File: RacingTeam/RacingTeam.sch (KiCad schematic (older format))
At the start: 78 parts, among them J1 BusIn, J10 BatteryIn, J11 ShutdownIn, J2 Conn_01x01, J3 Conn_01x01, J4 Conn_01x01, J5 Conn_01x01, J6 PreCharge Relay Out, J7 AIROut, J8 Discharge Relay Out, J9 PCB OUT, Q1 TP0610T, Q2 2N7002, Q3 2N7002, Q4 2N7002, Q5 2N7002, Q6 TP0610T, Q7 2N7002, Q8 TP0610T, U1 LM311, U2 LM311, U3 4N35, U6 NE555D

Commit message: Update RacingTeam.kicad_pcb, RacingTeam.kicad_pcb-bak, and 3 more files...
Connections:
- net PrechargeTP+ is gone; now on net PrechargeRef: D1.1 (K), F6.1, F6.2, J3.1 (Pin_1), R10.2, R11.1, R16.2
- net TSALREF: now also F2.2, R1.1, R2.2; no longer F2.1, J4.1 (Pin_1), R19.2
- net 555Reset: now reaches Q5.3 (D), Q6.1 (G), R27.2, U6.4 (R)
- net 555Trigger: now reaches C8.1, R30.2, U6.2 (TR), U6.6 (THR)
- net 555Ouput: now reaches Q7.2 (G), U6.3 (Q)
- net 555DischargePullup: now reaches R29.2, R30.1, U6.7 (DIS)
- net 555Drive: now reaches Q7.3 (D), Q8.1 (G), R31.2
- net OBLEDResistorRed: now reaches D8.1 (K), R32.1
- net OBLEDRed: now reaches D8.2 (A), JP2.2
- net TSALRef: now reaches F1.2, R14.2, R15.1
- net PrechargeRelayOut: now reaches D3.2 (A), J6.2 (Pin_2), R21.2
- net AIROut: now reaches D4.2 (A), J7.2 (Pin_2), R23.2
- net OBLEDResistorGreen: now reaches D6.1 (K), R28.1
- net OBLEDGreen: now reaches D6.2 (A), JP1.2
- net Ec3Out+: now reaches F3.2, PS1.6 (+VOUT)
- net DischargeIn: now reaches D5.1 (K), Q3.1 (S), Q4.1 (S)
- net DischargeIn: now also J8.2 (Pin_2); no longer J8.1 (Pin_1)
- net DischargeOut: now reaches D5.2 (A), R25.2
- net DischargeOut: now also J8.1 (Pin_1); no longer J8.2 (Pin_2)
- new net TSALCommon: F2.1, J4.1 (Pin_1), R19.2
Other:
- note added: "How drive?\n"
- moved on the sheet: F1, F3, R28, R32
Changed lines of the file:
@@
 	750  3300 750  3350
 Wire Wire Line
-	1300 2250 1400 2250
+	1300 2250 1450 2250
 Wire Wire Line
 	2300 2250 2300 2700
@@
 	1    0    0    -1
 $EndComp
-Text Label 1550 3300 0    25   ~ 0
+Text Label 750  3300 0    25   ~ 0
 TSALREF
 Text Label 1650 2250 0    25   ~ 0
@@
 Text Label 3400 3300 0    25   ~ 0
 LM311V-
-Text Label 3900 2600 1    25   ~ 0
-LM311Power+
-Text Label 4250 3350 2    25   ~ 0
-LM311Power-
 $Comp
 L RacingTeamPCB:C C3
@@
 	1    0    0    -1
 $EndComp
-Text Label 5150 2900 0    25   ~ 0
-OptoIn
 Text Label 4600 3000 0    25   ~ 0
 CompOut
@@
 L RacingTeamPCB:GLV- #U010
 U 1 1 623FD30F
-P 8500 4550
-F 0 "#U010" H 8422 4504 50  0001 R CNN
-F 1 "GLV-" H 8600 4400 50  0000 R CNN
-F 2 "" H 8500 4550 50  0001 C CNN
-F 3 "" H 8500 4550 50  0001 C CNN
-	1    8500 4550
+P 8500 4650
+F 0 "#U010" H 8422 4604 50  0001 R CNN
+F 1 "GLV-" H 8600 4500 50  0000 R CNN
+F 2 "" H 8500 4650 50  0001 C CNN
+F 3 "" H 8500 4650 50  0001 C CNN
+	1    8500 4650
 	1    0    0    -1
 $EndComp
@@
 	8650 5950 8650 6050
 Wire Wire Line
-	8650 6050 8900 6050
+	8650 6050 8800 6050
 Wire Wire Line
 	8650 6250 8650 6150
@@
 L Connector:Screw_Terminal_01x02 J8
 U 1 1 625195F4
-P 6300 5750
-F 0 "J8" H 6380 5742 50  0000 L CNN
-F 1 "Discharge Relay Out" H 6380 5651 50  0000 L CNN
-F 2 "GRC2022:CUI_TBL001-500-02GY-2GY" H 6300 5750 50  0001 C CNN
-F 3 "~" H 6300 5750 50  0001 C CNN
-	1    6300 5750
-	1    0    0    -1
+P 6300 5850
+F 0 "J8" H 6380 5842 50  0000 L CNN
+F 1 "Discharge Relay Out" H 6380 5751 50  0000 L CNN
+F 2 "GRC2022:CUI_TBL001-500-02GY-2GY" H 6300 5850 50  0001 C CNN
+F 3 "~" H 6300 5850 50  0001 C CNN
+	1    6300 5850
+	1    0    0    1
 $EndComp
 $Comp
@@
 L Device:Fuse_Small F3
 U 1 1 6247AD1E
-P 9000 6050
-F 0 "F3" H 9000 6143 50  0000 C CNN
-F 1 "Fuse_Small" H 9000 6144 50  0001 C CNN
-F 2 "GRC2022:FUSE_0154004.DRTL" H 9000 6050 50  0001 C CNN
-F 3 "~" H 9000 6050 50  0001 C CNN
-	1    9000 6050
+P 8900 6050
+F 0 "F3" H 8900 6143 50  0000 C CNN
+F 1 "Fuse_Small" H 8900 6144 50  0001 C CNN
+F 2 "GRC2022:FUSE_0154004.DRTL" H 8900 6050 50  0001 C CNN
+F 3 "~" H 8900 6050 50  0001 C CNN
+	1    8900 6050
 	1    0    0    -1
 $EndComp
 Wire Wire Line
-	9100 6050 9200 6050
+	9000 6050 9200 6050
 $Comp
 L Device:Fuse_Small F5
@@
 L Device:Fuse_Small F1
 U 1 1 62489769
-P 1500 2250
-F 0 "F1" H 1500 2300 50  0000 C CNN
-F 1 "Fuse_Small" H 1150 2450 50  0001 C CNN
-F 2 "GRC2022:FUSE_0154004.DRTL" H 1500 2250 50  0001 C CNN
-F 3 "~" H 1500 2250 50  0001 C CNN
-	1    1500 2250
+P 1550 2250
+F 0 "F1" H 1550 2300 50  0000 C CNN
+F 1 "Fuse_Small" H 1200 2450 50  0001 C CNN
+F 2 "GRC2022:FUSE_0154004.DRTL" H 1550 2250 50  0001 C CNN
+F 3 "~" H 1550 2250 50  0001 C CNN
+	1    1550 2250
 	-1   0    0    -1
 $EndComp
 Wire Wire Line
-	1600 2250 2050 2250
+	1650 2250 2050 2250
 Wire Wire Line
 	8650 6150 9200 6150
@@
 L RacingTeamPCB:R R28
 U 1 1 623FD309
-P 8500 4400
-F 0 "R28" H 8700 4500 50  0000 C CNN
-F 1 "499Ω" H 8700 4400 50  0000 C CNN
-F 2 "GRC2022:R_0603" V 8430 4400 50  0001 C CNN
-F 3 "~" H 8500 4400 50  0001 C CNN
-	1    8500 4400
+P 8500 4500
+F 0 "R28" H 8700 4600 50  0000 C CNN
+F 1 "499Ω" H 8700 4500 50  0000 C CNN
+F 2 "GRC2022:R_0603" V 8430 4500 50  0001 C CNN
+F 3 "~" H 8500 4500 50  0001 C CNN
+	1    8500 4500
 	1    0    0    -1
 $EndComp
@@
 L RacingTeamPCB:GLV- #U015
 U 1 1 61E548C8
-P 10800 2400
-F 0 "#U015" H 10722 2354 50  0001 R CNN
-F 1 "GLV-" H 10900 2250 50  0000 R CNN
-F 2 "" H 10800 2400 50  0001 C CNN
-F 3 "" H 10800 2400 50  0001 C CNN
-	1    10800 2400
+P 10800 2500
+F 0 "#U015" H 10722 2454 50  0001 R CNN
+F 1 "GLV-" H 10900 2350 50  0000 R CNN
+F 2 "" H 10800 2500 50  0001 C CNN
+F 3 "" H 10800 2500 50  0001 C CNN
+	1    10800 2500
 	1    0    0    -1
 $EndComp
@@
 L RacingTeamPCB:R R32
 U 1 1 61E53E52
-P 10800 2250
-F 0 "R32" H 10600 2250 50  0000 C CNN
-F 1 "499Ω" H 10600 2150 50  0000 C CNN
-F 2 "GRC2022:R_0603" V 10730 2250 50  0001 C CNN
-F 3 "~" H 10800 2250 50  0001 C CNN
-	1    10800 2250
+P 10800 2350
+F 0 "R32" H 10600 2350 50  0000 C CNN
+F 1 "499Ω" H 10600 2250 50  0000 C CNN
+F 2 "GRC2022:R_0603" V 10730 2350 50  0001 C CNN
+F 3 "~" H 10800 2350 50  0001 C CNN
+	1    10800 2350
 	1    0    0    -1
 $EndComp
@@
 Text Label 1550 7100 0    25   ~ 0
 PrechargeTP-
-Text Label 1550 6500 0    25   ~ 0
-PrechargeTP+
+Text Label 1250 5650 0    25   ~ 0
+PrechargeRef
 Text Label 1000 7100 0    25   ~ 0
 PrechargeRef
@@
 Text GLabel 8650 6150 0    25   Input ~ 0
 Shutdown-
+Text Label 1550 6300 1    25   ~ 0
+PrechargeTP+
+Text Label 1300 2250 0    25   ~ 0
+TSALRef
+Text Label 1500 3300 0    25   ~ 0
+TSALCommon
+Text Label 6900 1950 0    25   ~ 0
+555Reset
+Text Label 8700 1950 0    25   ~ 0
+555Trigger
+Text Label 9050 1450 0    25   ~ 0
+555DischargePullup
+Text Label 7000 1650 0    25   ~ 0
+555Bypass
+Text Label 8800 1550 0    25   ~ 0
+555Ouput
+Text Label 9750 1250 0    25   ~ 0
+555Drive
+Text Label 10800 1800 0    25   ~ 0
+OBLEDRed
+Text Label 10800 2200 0    25   ~ 0
+OBLEDResistorRed
+Wire Wire Line
+	10800 2100 10800 2200
+Text Label 8400 3950 0    25   ~ 0
+OBLEDGreen
+Text Label 8500 4350 0    25   ~ 0
+OBLEDResistorGreen
+Wire Wire Line
+	8500 4250 8500 4350
+Text Label 6100 5450 0    25   ~ 0
+DischargeIn
+Text Label 6100 6000 0    25   ~ 0
+DischargeOut
+Text Label 4550 6750 0    25   ~ 0
+AIROut
+Text Label 3650 5750 0    25   ~ 0
+PrechargeRelayOut
+Text Notes 2700 6400 0    25   ~ 0
+How drive?\n
+Text Label 9050 6050 0    25   ~ 0
+Ec3Out+
 $EndSCHEMATC

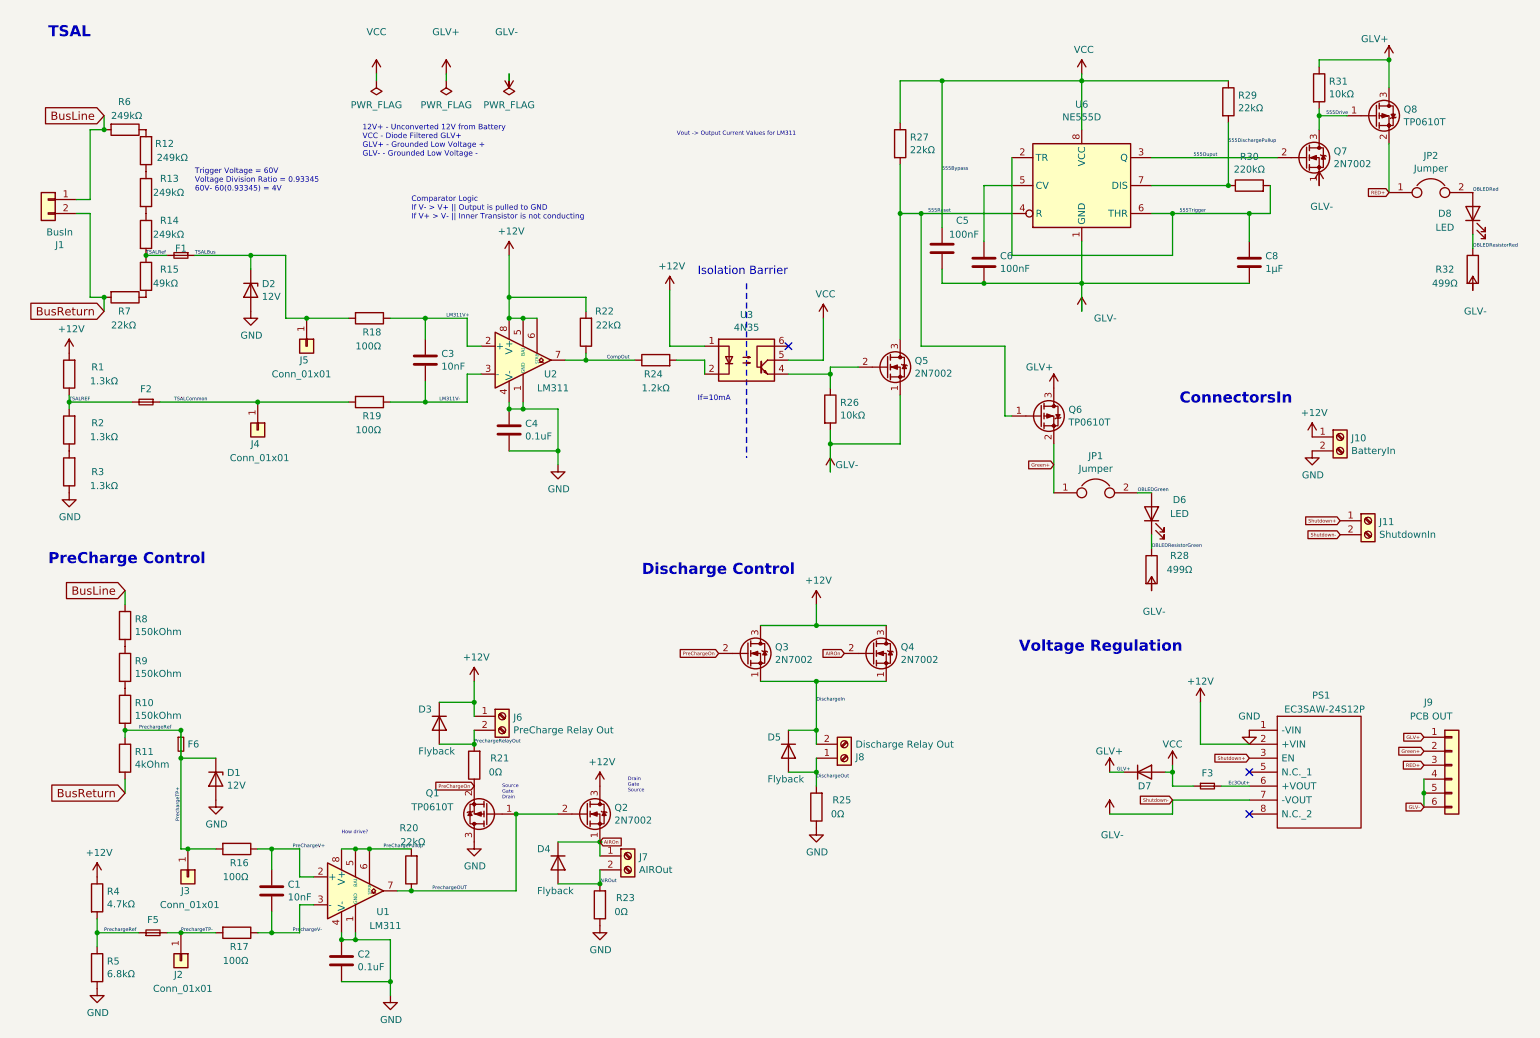
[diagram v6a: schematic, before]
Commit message: Update RacingTeamPCB.dcm, RacingTeamPCB.lib, and 6 more files...
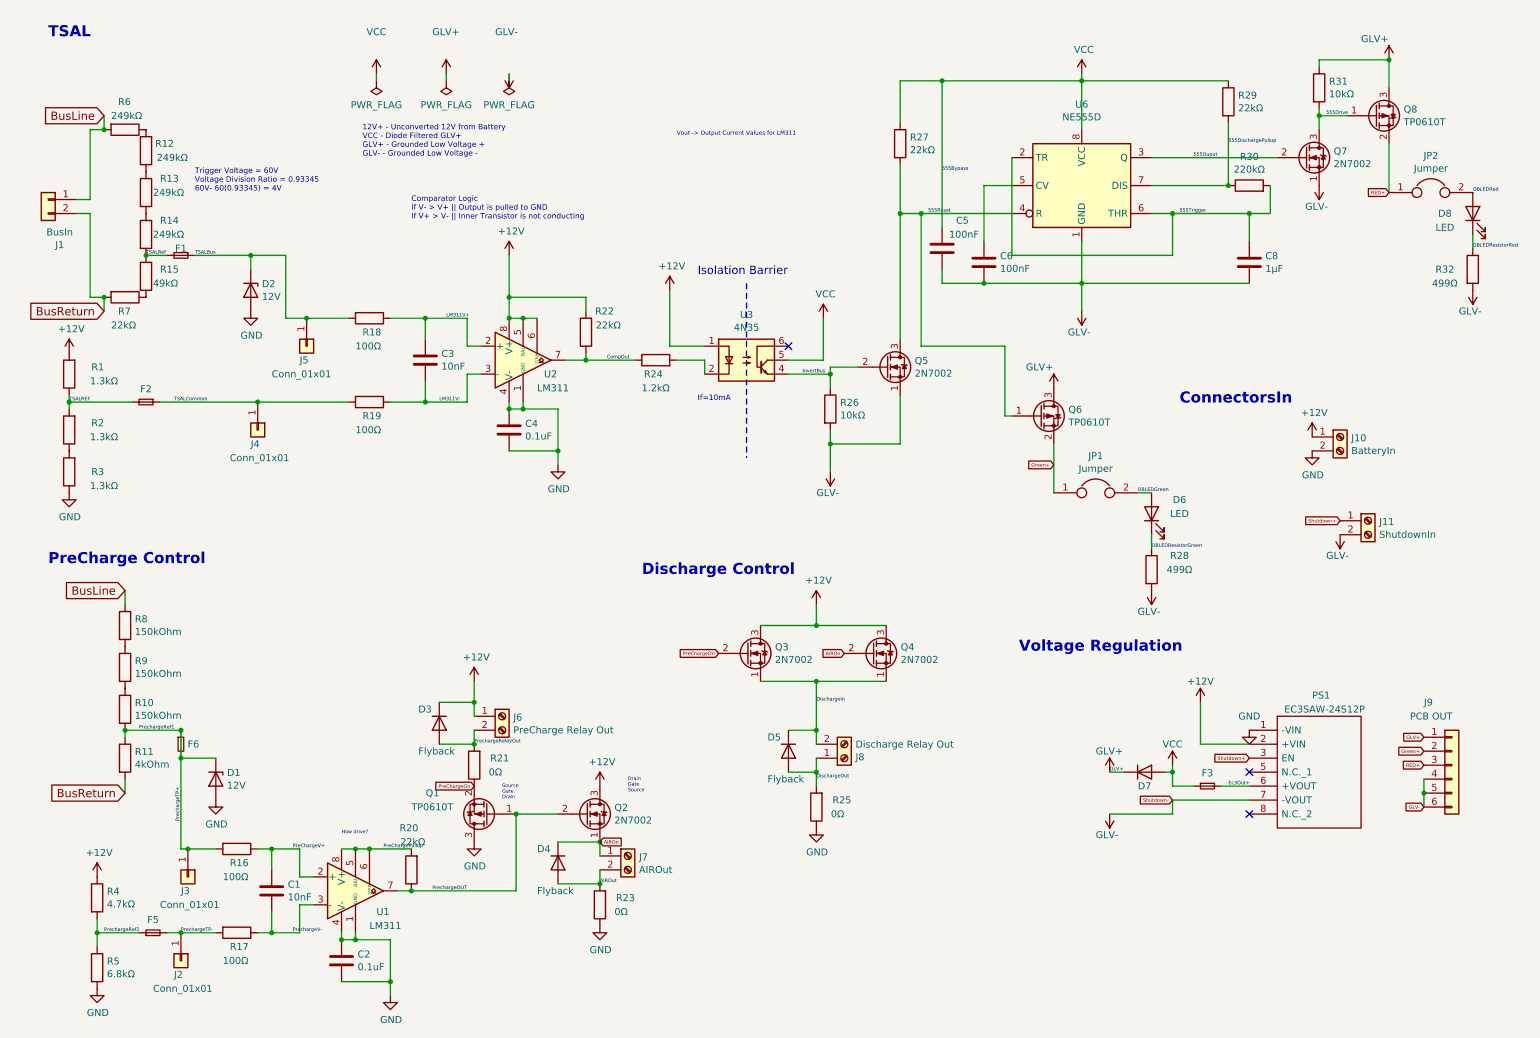
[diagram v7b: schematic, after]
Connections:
- net InvertBus: now reaches Q5.2 (G), R26.1, U3.4
- net PrechargeRef renamed PrechargeRef1
- net PrechargeRef1: no longer F5.1, R4.2, R5.1
- new net PrechargeRef2: F5.1, R4.2, R5.1
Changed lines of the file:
@@
 Wire Wire Line
 	8500 1550 9400 1550
-$Comp
-L RacingTeamPCB:GLV- #U011
-U 1 1 61E50A07
-P 9700 1750
-F 0 "#U011" H 9622 1704 50  0001 R CNN
-F 1 "GLV-" H 9800 1600 50  0000 R CNN
-F 2 "" H 9700 1750 50  0001 C CNN
-F 3 "" H 9700 1750 50  0001 C CNN
-	1    9700 1750
-	1    0    0    -1
-$EndComp
 Wire Wire Line
 	9700 1250 9700 1350
@@
 Green+
 $Comp
-L RacingTeamPCB:GLV- #U04
-U 1 1 61F703AB
-P 6200 3800
-F 0 "#U04" H 6200 3675 50  0001 C CNN
-F 1 "GLV-" H 6400 3850 50  0000 R CNN
-F 2 "" H 6200 3800 50  0001 C CNN
-F 3 "" H 6200 3800 50  0001 C CNN
-	1    6200 3800
-	1    0    0    -1
-$EndComp
-$Comp
 L power:GND #PWR06
 U 1 1 61DCC994
@@
 $EndComp
 $Comp
-L RacingTeamPCB:D D7
-U 1 1 621F41DC
-P 8450 5950
-F 0 "D7" H 8450 5850 50  0000 C CNN
-F 1 "D" H 8450 6076 50  0001 C CNN
-F 2 "GRC2022:SD0805S040S0R5" H 8450 5950 50  0001 C CNN
-F 3 "~" H 8450 5950 50  0001 C CNN
-	1    8450 5950
-	1    0    0    -1
-$EndComp
-$Comp
 L RacingTeamPCB:Conn_01x06 J9
 U 1 1 622055CC
@@
 	4550 6450 4550 6550
 $Comp
-L RacingTeamPCB:GLV- #U09
-U 1 1 621D6E85
-P 8200 6250
-F 0 "#U09" H 8122 6204 50  0001 R CNN
-F 1 "GLV-" H 8300 6100 50  0000 R CNN
-F 2 "" H 8200 6250 50  0001 C CNN
-F 3 "" H 8200 6250 50  0001 C CNN
-	1    8200 6250
-	1    0    0    -1
-$EndComp
-$Comp
-L RacingTeamPCB:GLV+ #U08
-U 1 1 62200FFB
-P 8200 5950
-F 0 "#U08" H 8278 5988 50  0001 L CNN
-F 1 "GLV+" H 8100 6100 50  0000 L CNN
-F 2 "" H 8200 5950 50  0001 C CNN
-F 3 "" H 8200 5950 50  0001 C CNN
-	1    8200 5950
-	1    0    0    -1
-$EndComp
-$Comp
 L RacingTeamPCB:GLV+ #U05
 U 1 1 61E73533
@@
 	0    -1   -1   0
 $EndComp
-$Comp
-L RacingTeamPCB:GLV- #U010
-U 1 1 623FD30F
-P 8500 4650
-F 0 "#U010" H 8422 4604 50  0001 R CNN
-F 1 "GLV-" H 8600 4500 50  0000 R CNN
-F 2 "" H 8500 4650 50  0001 C CNN
-F 3 "" H 8500 4650 50  0001 C CNN
-	1    8500 4650
-	1    0    0    -1
-$EndComp
 Wire Wire Line
 	7800 3600 7800 3950
@@
 $EndComp
 $Comp
-L RacingTeamPCB:GLV- #U015
-U 1 1 61E548C8
-P 10800 2500
-F 0 "#U015" H 10722 2454 50  0001 R CNN
-F 1 "GLV-" H 10900 2350 50  0000 R CNN
-F 2 "" H 10800 2500 50  0001 C CNN
-F 3 "" H 10800 2500 50  0001 C CNN
-	1    10800 2500
-	1    0    0    -1
-$EndComp
-$Comp
 L RacingTeamPCB:R R32
 U 1 1 61E53E52
@@
 PrechargeTP-
 Text Label 1250 5650 0    25   ~ 0
-PrechargeRef
+PrechargeRef1
 Text Label 1000 7100 0    25   ~ 0
-PrechargeRef
+PrechargeRef2
 Text GLabel 5400 5100 0    25   Input ~ 0
 PreChargeOn
@@
 AIROn
 Connection ~ 10200 850
-$Comp
-L RacingTeamPCB:GLV- #U07
-U 1 1 61E5FC5D
-P 8000 2650
-F 0 "#U07" H 7922 2604 50  0001 R CNN
-F 1 "GLV-" H 8250 2600 50  0000 R CNN
-F 2 "" H 8000 2650 50  0001 C CNN
-F 3 "" H 8000 2650 50  0001 C CNN
-	1    8000 2650
-	1    0    0    -1
-$EndComp
 Wire Wire Line
 	8000 2450 8000 2650
@@
 Wire Wire Line
 	8200 6250 8650 6250
-Text Label 8250 5950 0    25   ~ 0
-GLV+
 $Comp
 L Connector:Screw_Terminal_01x02 J10
@@
 Text GLabel 9850 4150 0    25   Input ~ 0
 Shutdown+
-Text GLabel 9850 4250 0    25   Input ~ 0
-Shutdown-
 Text Notes 8700 3450 0    79   ~ 16
 ConnectorsIn\n\n
-Text GLabel 8650 6150 0    25   Input ~ 0
-Shutdown-
 Text Label 1550 6300 1    25   ~ 0
 PrechargeTP+
@@
 Text Label 9050 6050 0    25   ~ 0
 Ec3Out+
+$Comp
+L RacingTeamPCB:GLV- #U0101
+U 1 1 62490A8F
+P 9850 4250
+F 0 "#U0101" H 9772 4204 50  0001 R CNN
+F 1 "GLV-" H 9950 4400 50  0000 R CNN
+F 2 "" H 9850 4250 50  0001 C CNN
+F 3 "" H 9850 4250 50  0001 C CNN
+	1    9850 4250
+	-1   0    0    1
+$EndComp
+$Comp
+L RacingTeamPCB:GLV- #U09
+U 1 1 621D6E85
+P 8200 6250
+F 0 "#U09" H 8122 6204 50  0001 R CNN
+F 1 "GLV-" H 8300 6400 50  0000 R CNN
+F 2 "" H 8200 6250 50  0001 C CNN
+F 3 "" H 8200 6250 50  0001 C CNN
+	1    8200 6250
+	-1   0    0    1
+$EndComp
+$Comp
+L RacingTeamPCB:GLV- #U015
+U 1 1 61E548C8
+P 10800 2500
+F 0 "#U015" H 10722 2454 50  0001 R CNN
+F 1 "GLV-" H 10900 2650 50  0000 R CNN
+F 2 "" H 10800 2500 50  0001 C CNN
+F 3 "" H 10800 2500 50  0001 C CNN
+	1    10800 2500
+	-1   0    0    1
+$EndComp
+$Comp
+L RacingTeamPCB:GLV- #U011
+U 1 1 61E50A07
+P 9700 1750
+F 0 "#U011" H 9622 1704 50  0001 R CNN
+F 1 "GLV-" H 9800 1900 50  0000 R CNN
+F 2 "" H 9700 1750 50  0001 C CNN
+F 3 "" H 9700 1750 50  0001 C CNN
+	1    9700 1750
+	-1   0    0    1
+$EndComp
+$Comp
+L RacingTeamPCB:GLV- #U07
+U 1 1 61E5FC5D
+P 8000 2650
+F 0 "#U07" H 7922 2604 50  0001 R CNN
+F 1 "GLV-" H 8100 2800 50  0000 R CNN
+F 2 "" H 8000 2650 50  0001 C CNN
+F 3 "" H 8000 2650 50  0001 C CNN
+	1    8000 2650
+	-1   0    0    1
+$EndComp
+$Comp
+L RacingTeamPCB:GLV+ #U08
+U 1 1 62200FFB
+P 8200 5950
+F 0 "#U08" H 8278 5988 50  0001 L CNN
+F 1 "GLV+" H 8100 6100 50  0000 L CNN
+F 2 "" H 8200 5950 50  0001 C CNN
+F 3 "" H 8200 5950 50  0001 C CNN
+	1    8200 5950
+	1    0    0    -1
+$EndComp
+$Comp
+L RacingTeamPCB:GLV- #U010
+U 1 1 623FD30F
+P 8500 4650
+F 0 "#U010" H 8422 4604 50  0001 R CNN
+F 1 "GLV-" H 8600 4800 50  0000 R CNN
+F 2 "" H 8500 4650 50  0001 C CNN
+F 3 "" H 8500 4650 50  0001 C CNN
+	1    8500 4650
+	-1   0    0    1
+$EndComp
+$Comp
+L RacingTeamPCB:D D7
+U 1 1 621F41DC
+P 8450 5950
+F 0 "D7" H 8450 5850 50  0000 C CNN
+F 1 "D" H 8450 6076 50  0001 C CNN
+F 2 "GRC2022:SD0805S040S0R5" H 8450 5950 50  0001 C CNN
+F 3 "~" H 8450 5950 50  0001 C CNN
+	1    8450 5950
+	1    0    0    -1
+$EndComp
+Text Label 8200 5950 0    25   ~ 0
+GLV+
+$Comp
+L RacingTeamPCB:GLV- #U04
+U 1 1 61F703AB
+P 6200 3800
+F 0 "#U04" H 6200 3675 50  0001 C CNN
+F 1 "GLV-" H 6300 3950 50  0000 R CNN
+F 2 "" H 6200 3800 50  0001 C CNN
+F 3 "" H 6200 3800 50  0001 C CNN
+	1    6200 3800
+	-1   0    0    1
+$EndComp
+Text GLabel 8650 6150 0    25   Input ~ 0
+Shutdown-
+Text Label 6000 3100 0    25   ~ 0
+InvertBus
 $EndSCHEMATC

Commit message: Update PCBBom.xlsx, RacingTeam.kicad_pcb, and 4 more files...
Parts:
- added R33, R34, R35, R36: 0Ω, GRC2022:R_0805, symbol RacingTeamPCB:R
- J2, J3: value Conn_01x01 -> TestPoint
- J4, J5: value Conn_01x01 -> TestPin
- R10, R8, R9: value 150kOhm -> 150kΩ
- R11: value 4kOhm -> 4kΩ
- R20, R22: value 22kΩ -> 20kΩ
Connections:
- net TSALCommon is gone; now on net TSALRef: F2.1, J4.1 (Pin_1), R19.2
- net +12V: no longer D3.1 (K), J10.1 (Pin_1), J6.1 (Pin_1), PS1.2 (+VIN), Q2.3 (D), R4.1, U2.5 (BAL), U2.6 (STRB)
- net GND: no longer PS1.1 (-VIN)
- net PrechargeRef2: now also R36.1
- net PrechargeTP-: now also R36.2
- net Shutdown+: no longer J11.1 (Pin_1)
- net TSALRef: now also R34.1; no longer F1.2, R14.2, R15.1
- net TSALREFOut: now reaches R2.1, R3.2
- net TSALREFOut: now also F2.2, R34.2
- net 555DischargePullup renamed 555Discharge
- net 555Drive renamed 555DriveRED
- net 555Ouput renamed 555Output
- net CompOut renamed TSALCompOut
- net LM311V+ renamed TSAL_LM311V+
- net LM311V- renamed TSAL_LM311V-
- net PreChargePullup: no longer names the net of R20.2, U1.5 (BAL), U1.6 (STRB)
- net PreChargePullup: no longer U1.8 (V+)
- net PrechargeOUT renamed PrechargeCompOUT
- net PrechargeRef1 renamed PrechargeBus
- net PrechargeBus: now also R35.2; no longer F6.2, J3.1 (Pin_1), R16.2
- net TSALBus renamed BusRefTSAL
- net BusRefTSAL: now also R33.1
- net TSALREF: no longer names the net of R1.1, R2.2
- net TSALREF: no longer F2.2
- new net: U2.5 (BAL), U2.6 (STRB)
- new net: D3.1 (K), J6.1 (Pin_1)
- new net BusOutTSAL: F1.2, R14.2, R15.1, R33.2
- new net PrechargeTP+: F6.2, J3.1 (Pin_1), R16.2, R35.1
- new net Shutdown: J11.1 (Pin_1)
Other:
- note added: "Input from battery on GLV side\n\n"
- note removed: "How drive?\n"
- note removed: "Vout -> Output Current Values for LM311\n"
- moved on the sheet: D1, F1, F2, F5, F6, R1, R2, R22, R3, R4, R5
